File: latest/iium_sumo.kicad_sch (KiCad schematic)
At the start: 55 parts, among them J1 I2C_VL53_1, J10 Cytron MD, J11 Cytron Start Module, J12 Conn_01x04, J13 Conn_01x04, J14 Conn_01x04, J15 EXTRA1, J16 Conn_01x02_Pin, J17 Conn_01x02_Pin, J18 UART1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

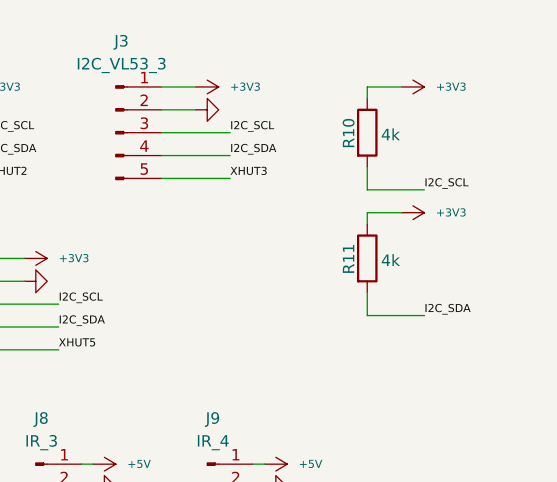
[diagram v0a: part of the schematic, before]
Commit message: Updated pull resisto
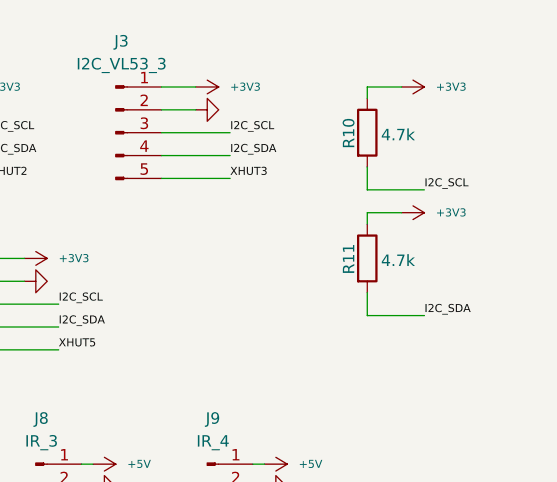
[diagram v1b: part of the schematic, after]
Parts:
- R10, R11: value 4k -> 4.7k
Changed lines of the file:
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@@
 			)
 		)
-		(property "Value" "4k"
+		(property "Value" "4.7k"
 			(at 260.604 38.354 0)
 			(show_name no)
@@
 			)
 		)
-		(property "Value" "4k"
+		(property "Value" "4.7k"
 			(at 260.604 24.384 0)
 			(show_name no)

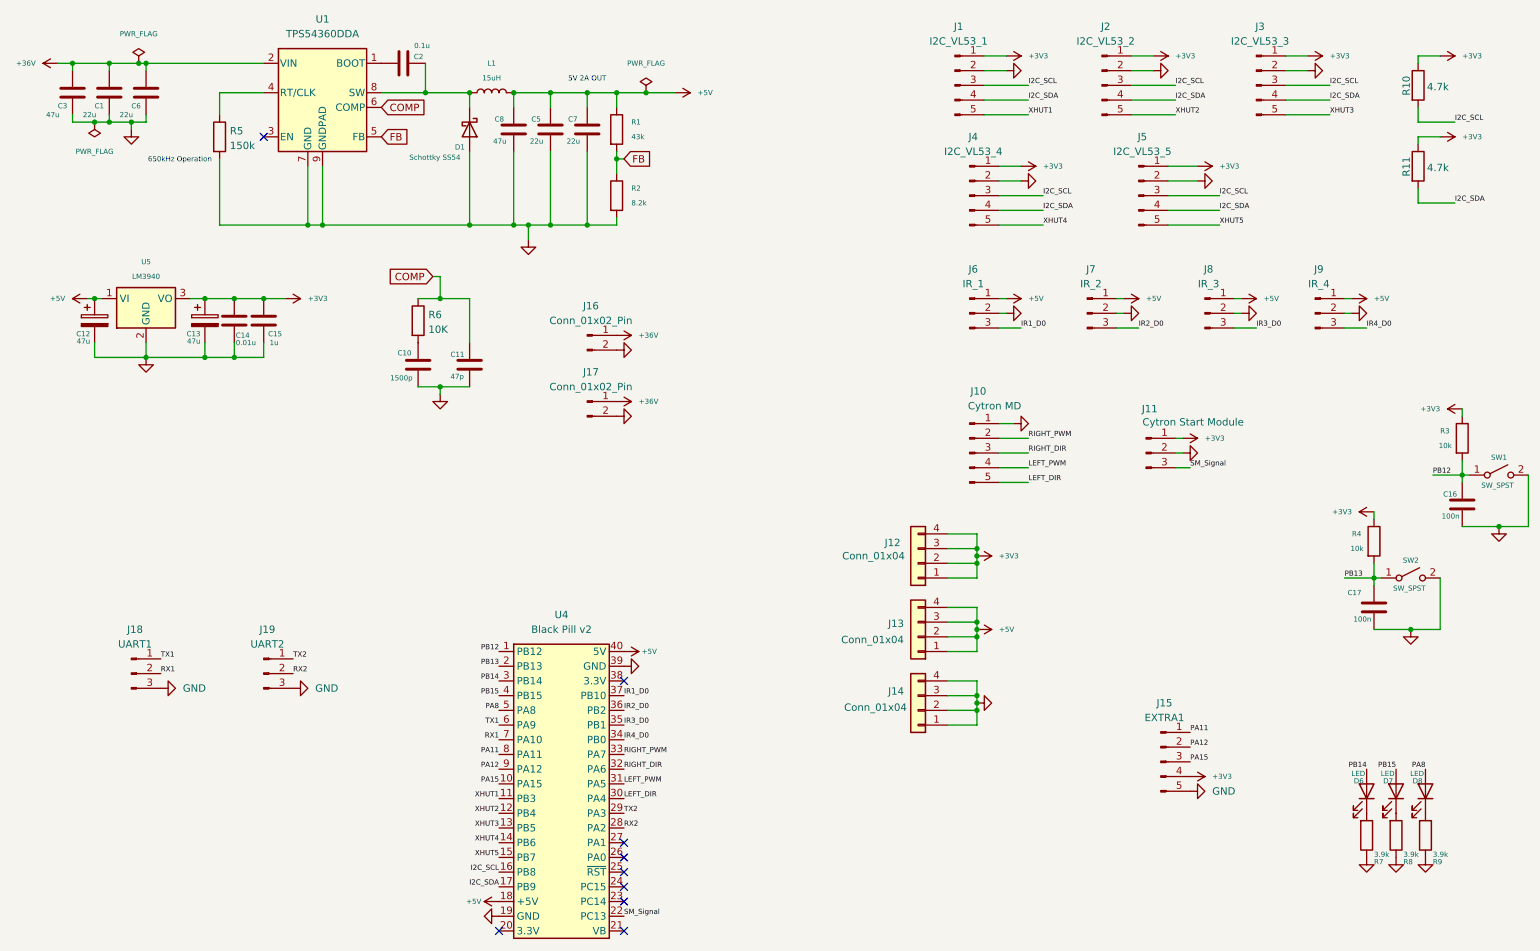
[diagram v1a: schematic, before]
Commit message: schematic update
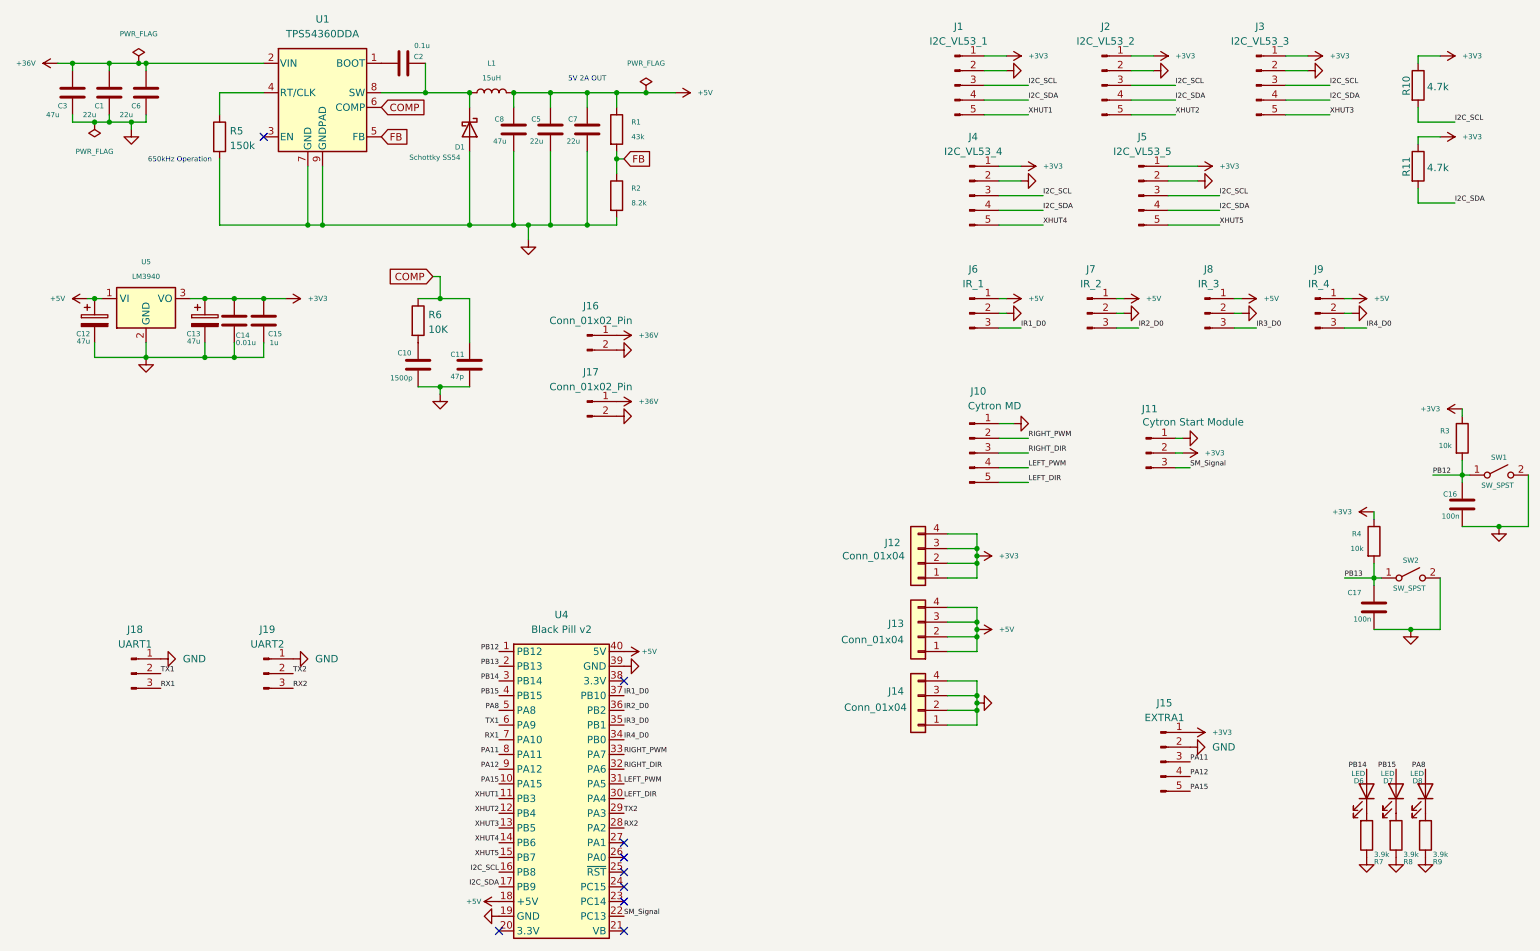
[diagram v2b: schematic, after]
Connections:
- net +3V3: now also J11.2 (Pin_2), J15.1 (Pin_1); no longer J11.1 (Pin_1), J15.4 (Pin_4)
- net GND: now also J11.1 (Pin_1), J15.2 (Pin_2), J18.1 (Pin_1), J19.1 (Pin_1); no longer J11.2 (Pin_2), J15.5 (Pin_5), J18.3 (Pin_3), J19.3 (Pin_3)
- net PA11: now also J15.3 (Pin_3); no longer J15.1 (Pin_1)
- net PA12: now also J15.4 (Pin_4); no longer J15.2 (Pin_2)
- net PA15: now also J15.5 (Pin_5); no longer J15.3 (Pin_3)
- net RX1: now also J18.3 (Pin_3); no longer J18.2 (Pin_2)
- net RX2: now also J19.3 (Pin_3); no longer J19.2 (Pin_2)
- net TX1: now also J18.2 (Pin_2); no longer J18.1 (Pin_1)
- net TX2: now also J19.2 (Pin_2); no longer J19.1 (Pin_1)
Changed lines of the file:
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@@
 	)
 	(label "RX2"
-		(at 64.77 125.73 0)
+		(at 64.77 128.27 0)
 		(effects
 			(font
@@
 	)
 	(label "TX1"
-		(at 41.91 123.19 0)
+		(at 41.91 125.73 0)
 		(effects
 			(font
@@
 	)
 	(label "PA11"
-		(at 219.71 135.89 0)
+		(at 219.71 140.97 0)
 		(effects
 			(font
@@
 	)
 	(label "TX2"
-		(at 64.77 123.19 0)
+		(at 64.77 125.73 0)
 		(effects
 			(font
@@
 	)
 	(label "RX1"
-		(at 41.91 125.73 0)
+		(at 41.91 128.27 0)
 		(effects
 			(font
@@
 	)
 	(label "PA15"
-		(at 219.71 140.97 0)
+		(at 219.71 146.05 0)
 		(effects
 			(font
@@
 	)
 	(label "PA12"
-		(at 219.71 138.43 0)
+		(at 219.71 143.51 0)
 		(effects
 			(font
@@
 	(symbol
 		(lib_id "power:GND")
-		(at 219.71 146.05 90)
+		(at 219.71 138.43 90)
 		(unit 1)
 		(body_style 1)
@@
 		(fields_autoplaced yes)
 		(property "Reference" "#PWR040"
-			(at 226.06 146.05 0)
+			(at 226.06 138.43 0)
 			(hide yes)
 			(show_name no)
@@
 		)
 		(property "Value" "GND"
-			(at 223.52 146.0499 90)
+			(at 223.52 138.4299 90)
 			(show_name no)
 			(do_not_autoplace no)
@@
 		)
 		(property "Footprint" ""
-			(at 219.71 146.05 0)
+			(at 219.71 138.43 0)
 			(hide yes)
 			(show_name no)
@@
 		)
 		(property "Datasheet" ""
-			(at 219.71 146.05 0)
+			(at 219.71 138.43 0)
 			(hide yes)
 			(show_name no)
@@
 		)
 		(property "Description" "Power symbol creates a global label with name \"GND\" , ground"
-			(at 219.71 146.05 0)
+			(at 219.71 138.43 0)
 			(hide yes)
 			(show_name no)
@@
 	(symbol
 		(lib_id "power:GND")
-		(at 41.91 128.27 90)
+		(at 41.91 123.19 90)
 		(unit 1)
 		(body_style 1)
@@
 		(fields_autoplaced yes)
 		(property "Reference" "#PWR08"
-			(at 48.26 128.27 0)
+			(at 48.26 123.19 0)
 			(hide yes)
 			(show_name no)
@@
 		)
 		(property "Value" "GND"
-			(at 45.72 128.2699 90)
+			(at 45.72 123.1899 90)
 			(show_name no)
 			(do_not_autoplace no)
@@
 		)
 		(property "Footprint" ""
-			(at 41.91 128.27 0)
+			(at 41.91 123.19 0)
 			(hide yes)
 			(show_name no)
@@
 		)
 		(property "Datasheet" ""
-			(at 41.91 128.27 0)
+			(at 41.91 123.19 0)
 			(hide yes)
 			(show_name no)
@@
 		)
 		(property "Description" "Power symbol creates a global label with name \"GND\" , ground"
-			(at 41.91 128.27 0)
+			(at 41.91 123.19 0)
 			(hide yes)
 			(show_name no)
@@
 	(symbol
 		(lib_id "power:GND")
-		(at 64.77 128.27 90)
+		(at 64.77 123.19 90)
 		(unit 1)
 		(body_style 1)
@@
 		(fields_autoplaced yes)
 		(property "Reference" "#PWR012"
-			(at 71.12 128.27 0)
+			(at 71.12 123.19 0)
 			(hide yes)
 			(show_name no)
@@
 		)
 		(property "Value" "GND"
-			(at 68.58 128.2699 90)
+			(at 68.58 123.1899 90)
 			(show_name no)
 			(do_not_autoplace no)
@@
 		)
 		(property "Footprint" ""
-			(at 64.77 128.27 0)
+			(at 64.77 123.19 0)
 			(hide yes)
 			(show_name no)
@@
 		)
 		(property "Datasheet" ""
-			(at 64.77 128.27 0)
+			(at 64.77 123.19 0)
 			(hide yes)
 			(show_name no)
@@
 		)
 		(property "Description" "Power symbol creates a global label with name \"GND\" , ground"
-			(at 64.77 128.27 0)
+			(at 64.77 123.19 0)
 			(hide yes)
 			(show_name no)
@@
 	(symbol
 		(lib_id "power:+3V3")
-		(at 219.71 143.51 270)
+		(at 219.71 135.89 270)
 		(unit 1)
 		(body_style 1)
@@
 		(fields_autoplaced yes)
 		(property "Reference" "#PWR039"
-			(at 215.9 143.51 0)
+			(at 215.9 135.89 0)
 			(hide yes)
 			(show_name no)
@@
 		)
 		(property "Value" "+3V3"
-			(at 223.52 143.51 90)
+			(at 223.52 135.89 90)
 			(show_name no)
 			(do_not_autoplace no)
@@
 		)
 		(property "Footprint" ""
-			(at 219.71 143.51 0)
+			(at 219.71 135.89 0)
 			(hide yes)
 			(show_name no)
@@
 		)
 		(property "Datasheet" ""
-			(at 219.71 143.51 0)
+			(at 219.71 135.89 0)
 			(hide yes)
 			(show_name no)
@@
 		)
 		(property "Description" "Power symbol creates a global label with name \"+3V3\""
-			(at 219.71 143.51 0)
+			(at 219.71 135.89 0)
 			(hide yes)
 			(show_name no)
@@
 	(symbol
 		(lib_id "power:+3V3")
-		(at 218.44 85.09 270)
+		(at 218.44 87.63 270)
 		(unit 1)
 		(body_style 1)
@@
 		(fields_autoplaced yes)
 		(property "Reference" "#PWR017"
-			(at 214.63 85.09 0)
+			(at 214.63 87.63 0)
 			(hide yes)
 			(show_name no)
@@
 		)
 		(property "Value" "+3V3"
-			(at 222.25 85.09 90)
+			(at 222.25 87.63 90)
 			(show_name no)
 			(do_not_autoplace no)
@@
 		)
 		(property "Footprint" ""
-			(at 218.44 85.09 0)
+			(at 218.44 87.63 0)
 			(hide yes)
 			(show_name no)
@@
 		)
 		(property "Datasheet" ""
-			(at 218.44 85.09 0)
+			(at 218.44 87.63 0)
 			(hide yes)
 			(show_name no)
@@
 		)
 		(property "Description" "Power symbol creates a global label with name \"+3V3\""
-			(at 218.44 85.09 0)
+			(at 218.44 87.63 0)
 			(hide yes)
 			(show_name no)
@@
 	(symbol
 		(lib_id "power:GND")
-		(at 218.44 87.63 90)
+		(at 218.44 85.09 90)
 		(unit 1)
 		(body_style 1)
@@
 		(fields_autoplaced yes)
 		(property "Reference" "#PWR019"
-			(at 224.79 87.63 0)
+			(at 224.79 85.09 0)
 			(hide yes)
 			(show_name no)
@@
 		)
 		(property "Value" "GND"
-			(at 222.25 87.6299 90)
+			(at 222.25 85.0899 90)
 			(hide yes)
 			(show_name no)
@@
 		)
 		(property "Footprint" ""
-			(at 218.44 87.63 0)
+			(at 218.44 85.09 0)
 			(hide yes)
 			(show_name no)
@@
 		)
 		(property "Datasheet" ""
-			(at 218.44 87.63 0)
+			(at 218.44 85.09 0)
 			(hide yes)
 			(show_name no)
@@
 		)
 		(property "Description" "Power symbol creates a global label with name \"GND\" , ground"
-			(at 218.44 87.63 0)
+			(at 218.44 85.09 0)
 			(hide yes)
 			(show_name no)

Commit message: touch up
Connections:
- net +36V: no longer C1.1, C3.1, C6.1, U1.2 (VIN)
- new net: C1.1, C3.1, C6.1, U1.2 (VIN)
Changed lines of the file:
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@@
 	)
 	(junction
-		(at 26.67 20.32)
+		(at 95.25 25.4)
 		(diameter 0)
 		(color 0 0 0 0)
 	)
 	(junction
-		(at 95.25 25.4)
+		(at 49.53 71.12)
 		(diameter 0)
 		(color 0 0 0 0)
 	)
 	(junction
-		(at 49.53 71.12)
+		(at 39.37 71.12)
 		(diameter 0)
 		(color 0 0 0 0)
 	)
 	(junction
-		(at 39.37 71.12)
+		(at 26.67 20.32)
 		(diameter 0)
 		(color 0 0 0 0)
@@
 	(wire
 		(pts
+			(xy 38.1 45.72) (xy 34.29 45.72)
+		)
+		(stroke
+			(width 0)
+			(type default)
+		)
+	)
+	(wire
+		(pts
 			(xy 259.08 30.48) (xy 265.43 30.48)
 		)
@@
 	(wire
 		(pts
+			(xy 19.05 20.32) (xy 26.67 20.32)
+		)
+		(stroke
+			(width 0)
+			(type default)
+		)
+	)
+	(wire
+		(pts
 			(xy 259.08 20.32) (xy 259.08 19.05)
 		)
@@
 	(wire
 		(pts
+			(xy 24.13 48.26) (xy 19.05 48.26)
+		)
+		(stroke
+			(width 0)
+			(type default)
+		)
+	)
+	(wire
+		(pts
 			(xy 67.31 48.26) (xy 69.85 48.26)
 		)
@@
 	(wire
 		(pts
-			(xy 24.13 20.32) (xy 26.67 20.32)
-		)
-		(stroke
-			(width 0)
-			(type default)
-		)
-	)
-	(wire
-		(pts
 			(xy 209.55 19.05) (xy 213.36 19.05)
 		)
@@
 	(wire
 		(pts
+			(xy 19.05 48.26) (xy 19.05 20.32)
+		)
+		(stroke
+			(width 0)
+			(type default)
+		)
+	)
+	(wire
+		(pts
 			(xy 49.53 71.12) (xy 54.61 71.12)
 		)
@@
 	(symbol
 		(lib_id "power:+12V")
-		(at 24.13 20.32 90)
+		(at 38.1 45.72 270)
 		(unit 1)
 		(body_style 1)
@@
 		(dnp no)
 		(property "Reference" "#PWR06"
-			(at 27.94 20.32 0)
+			(at 34.29 45.72 0)
 			(hide yes)
 			(show_name no)
@@
 		)
 		(property "Value" "+36V"
-			(at 20.32 20.3199 90)
+			(at 41.91 45.7201 90)
 			(show_name no)
 			(do_not_autoplace no)
@@
 		)
 		(property "Footprint" ""
-			(at 24.13 20.32 0)
+			(at 38.1 45.72 0)
 			(hide yes)
 			(show_name no)
@@
 		)
 		(property "Datasheet" ""
-			(at 24.13 20.32 0)
+			(at 38.1 45.72 0)
 			(hide yes)
 			(show_name no)
@@
 		)
 		(property "Description" "Power symbol creates a global label with name \"+12V\""
-			(at 24.13 20.32 0)
+			(at 38.1 45.72 0)
 			(hide yes)
 			(show_name no)

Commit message: drc cleared
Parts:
- added SW3: SW_SPDT, custom:SPDT_MT-1-102-A001-M200-RS, symbol Switch:SW_SPDT
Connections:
- net +36V: now also J16.2 (Pin_2), J17.2 (Pin_2), SW3.1 (A), SW3.3 (C); no longer J16.1 (Pin_1), J17.1 (Pin_1)
- net GND: now also J16.1 (Pin_1), J17.1 (Pin_1); no longer J16.2 (Pin_2), J17.2 (Pin_2)
- net at C1.1, C3.1, C6.1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: now also SW3.2 (B)
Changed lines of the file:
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@@
 	(wire
 		(pts
+			(xy 38.1 50.8) (xy 34.29 50.8)
+		)
+		(stroke
+			(width 0)
+			(type default)
+		)
+	)
+	(wire
+		(pts
 			(xy 90.17 76.2) (xy 95.25 76.2)
 		)
@@
 	(symbol
 		(lib_id "power:GND")
-		(at 120.65 81.28 90)
+		(at 120.65 78.74 90)
 		(unit 1)
 		(body_style 1)
@@
 		(fields_autoplaced yes)
 		(property "Reference" "#PWR046"
-			(at 127 81.28 0)
+			(at 127 78.74 0)
 			(hide yes)
 			(show_name no)
@@
 		)
 		(property "Value" "GND"
-			(at 124.46 81.2799 90)
+			(at 124.46 78.7399 90)
 			(hide yes)
 			(show_name no)
@@
 		)
 		(property "Footprint" ""
-			(at 120.65 81.28 0)
+			(at 120.65 78.74 0)
 			(hide yes)
 			(show_name no)
@@
 		)
 		(property "Datasheet" ""
-			(at 120.65 81.28 0)
+			(at 120.65 78.74 0)
 			(hide yes)
 			(show_name no)
@@
 		)
 		(property "Description" "Power symbol creates a global label with name \"GND\" , ground"
-			(at 120.65 81.28 0)
+			(at 120.65 78.74 0)
 			(hide yes)
 			(show_name no)
@@
 	)
 	(symbol
+		(lib_id "power:+12V")
+		(at 38.1 50.8 270)
+		(unit 1)
+		(body_style 1)
+		(exclude_from_sim no)
+		(in_bom yes)
+		(on_board yes)
+		(in_pos_files yes)
+		(dnp no)
+		(property "Reference" "#PWR049"
+			(at 34.29 50.8 0)
+			(hide yes)
+			(show_name no)
+			(do_not_autoplace no)
+			(effects
+				(font
+					(size 0.889 0.889)
+				)
+			)
+		)
+		(property "Value" "+36V"
+			(at 41.91 50.8001 90)
+			(show_name no)
+			(do_not_autoplace no)
+			(effects
+				(font
+					(size 0.889 0.889)
+				)
+				(justify left)
+			)
+		)
+		(property "Footprint" ""
+			(at 38.1 50.8 0)
+			(hide yes)
+			(show_name no)
+			(do_not_autoplace no)
+			(effects
+				(font
+					(size 0.889 0.889)
+				)
+			)
+		)
+		(property "Datasheet" ""
+			(at 38.1 50.8 0)
+			(hide yes)
+			(show_name no)
+			(do_not_autoplace no)
+			(effects
+				(font
+					(size 0.889 0.889)
+				)
+			)
+		)
+		(property "Description" "Power symbol creates a global label with name \"+12V\""
+			(at 38.1 50.8 0)
+			(hide yes)
+			(show_name no)
+			(do_not_autoplace no)
+			(effects
+				(font
+					(size 0.889 0.889)
+				)
+			)
+		)
+		(pin "1"
+		)
+		(instances
+			(project "iium_sumo"
+				(path "/70a47adf-789d-4812-99b3-df06d1ca2237"
+					(reference "#PWR049")
+					(unit 1)
+				)
+			)
+		)
+	)
+	(symbol
 		(lib_id "power:+3V3")
 		(at 247.65 60.96 270)
@@
 	(symbol
 		(lib_id "power:GND")
-		(at 120.65 69.85 90)
+		(at 120.65 67.31 90)
 		(unit 1)
 		(body_style 1)
@@
 		(fields_autoplaced yes)
 		(property "Reference" "#PWR020"
-			(at 127 69.85 0)
+			(at 127 67.31 0)
 			(hide yes)
 			(show_name no)
@@
 		)
 		(property "Value" "GND"
-			(at 124.46 69.8499 90)
+			(at 124.46 67.3099 90)
 			(hide yes)
 			(show_name no)
@@
 		)
 		(property "Footprint" ""
-			(at 120.65 69.85 0)
+			(at 120.65 67.31 0)
 			(hide yes)
 			(show_name no)
@@
 		)
 		(property "Datasheet" ""
-			(at 120.65 69.85 0)
+			(at 120.65 67.31 0)
 			(hide yes)
 			(show_name no)
@@
 		)
 		(property "Description" "Power symbol creates a global label with name \"GND\" , ground"
-			(at 120.65 69.85 0)
+			(at 120.65 67.31 0)
 			(hide yes)
 			(show_name no)
@@
 	)
 	(symbol
+		(lib_id "Switch:SW_SPDT")
+		(at 29.21 48.26 0)
+		(unit 1)
+		(body_style 1)
+		(exclude_from_sim no)
+		(in_bom yes)
+		(on_board yes)
+		(in_pos_files yes)
+		(dnp no)
+		(fields_autoplaced yes)
+		(property "Reference" "SW3"
+			(at 29.21 39.37 0)
+			(show_name no)
+			(do_not_autoplace no)
+			(effects
+				(font
+					(size 1.27 1.27)
+				)
+			)
+		)
+		(property "Value" "SW_SPDT"
+			(at 29.21 41.91 0)
+			(show_name no)
+			(do_not_autoplace no)
+			(effects
+				(font
+					(size 1.27 1.27)
+				)
+			)
+		)
+		(property "Footprint" "custom:SPDT_MT-1-102-A001-M200-RS"
+			(at 29.21 48.26 0)
+			(hide yes)
+			(show_name no)
+			(do_not_autoplace no)
+			(effects
+				(font
+					(size 1.27 1.27)
+				)
+			)
+		)
+		(property "Datasheet" ""
+			(at 29.21 55.88 0)
+			(hide yes)
+			(show_name no)
+			(do_not_autoplace no)
+			(effects
+				(font
+					(size 1.27 1.27)
+				)
+			)
+		)
+		(property "Description" "Switch, single pole double throw"
+			(at 29.21 48.26 0)
+			(hide yes)
+			(show_name no)
+			(do_not_autoplace no)
+			(effects
+				(font
+					(size 1.27 1.27)
+				)
+			)
+		)
+		(pin "1"
+		)
+		(pin "3"
+		)
+		(pin "2"
+		)
+		(instances
+			(project "iium_sumo"
+				(path "/70a47adf-789d-4812-99b3-df06d1ca2237"
+					(reference "SW3")
+					(unit 1)
+				)
+			)
+		)
+	)
+	(symbol
 		(lib_id "Connector:Conn_01x03_Pin")
 		(at 201.93 63.5 0)
@@
 	(symbol
 		(lib_id "power:+12V")
-		(at 120.65 67.31 270)
+		(at 120.65 69.85 270)
 		(unit 1)
 		(body_style 1)
@@
 		(dnp no)
 		(property "Reference" "#PWR016"
-			(at 116.84 67.31 0)
+			(at 116.84 69.85 0)
 			(hide yes)
 			(show_name no)
@@
 		)
 		(property "Value" "+36V"
-			(at 124.46 67.3101 90)
+			(at 124.46 69.8501 90)
 			(show_name no)
 			(do_not_autoplace no)
@@
 		)
 		(property "Footprint" ""
-			(at 120.65 67.31 0)
+			(at 120.65 69.85 0)
 			(hide yes)
 			(show_name no)
@@
 		)
 		(property "Datasheet" ""
-			(at 120.65 67.31 0)
+			(at 120.65 69.85 0)
 			(hide yes)
 			(show_name no)
@@
 		)
 		(property "Description" "Power symbol creates a global label with name \"+12V\""
-			(at 120.65 67.31 0)
+			(at 120.65 69.85 0)
 			(hide yes)
 			(show_name no)
@@
 	(symbol
 		(lib_id "power:+12V")
-		(at 120.65 78.74 270)
+		(at 120.65 81.28 270)
 		(unit 1)
 		(body_style 1)
@@
 		(dnp no)
 		(property "Reference" "#PWR045"
-			(at 116.84 78.74 0)
+			(at 116.84 81.28 0)
 			(hide yes)
 			(show_name no)
@@
 		)
 		(property "Value" "+36V"
-			(at 124.46 78.7401 90)
+			(at 124.46 81.2801 90)
 			(show_name no)
 			(do_not_autoplace no)
@@
 		)
 		(property "Footprint" ""
-			(at 120.65 78.74 0)
+			(at 120.65 81.28 0)
 			(hide yes)
 			(show_name no)
@@
 		)
 		(property "Datasheet" ""
-			(at 120.65 78.74 0)
+			(at 120.65 81.28 0)
 			(hide yes)
 			(show_name no)
@@
 		)
 		(property "Description" "Power symbol creates a global label with name \"+12V\""
-			(at 120.65 78.74 0)
+			(at 120.65 81.28 0)
 			(hide yes)
 			(show_name no)
